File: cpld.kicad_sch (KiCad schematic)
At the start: 30 parts, among them IC1 MCP1726-3302E_SN, IC2 EPM3064ATC44-7N, J1 USB_OTG, J2 INPUTS, J3 OUTPUTS, J4 Conn_ARM_JTAG_SWD_10, SW1 POWER_SW, SW2 SW_DIP_x01, SW3 SW_DIP_x01, SW4 SW_DIP_x01, SW5 SW_DIP_x01, Y1 ECS-2033-500-BN-TR3

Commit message: Added revision and title
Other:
- company: (none) -> AGH UST
- title: (none) -> ATPG with CPLD circuit
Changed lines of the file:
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@@
 (kicad_sch (version 20211123) (generator eeschema)
   (paper "A4")
+  (title_block
+    (title "ATPG with CPLD circuit")
+    (date "2022-08-07")
+    (rev "0.0.1")
+    (company "AGH UST")
+    (comment 1 "Author: Radosław Sajdak")
+  )
   (junction (at 104.14 177.8) (diameter 0) (color 0 0 0 0)
   )

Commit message: Final PCB
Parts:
- removed J2: INPUTS, Connector_PinSocket_2.54mm:PinSocket_2x16_P2.54mm_Vertical, symbol Connector_Generic:Conn_02x16_Top_Bottom
- removed J3: OUTPUTS, Connector_PinSocket_2.54mm:PinSocket_2x16_P2.54mm_Vertical, symbol Connector_Generic:Conn_02x16_Top_Bottom
- removed Y1: ECS-2033-500-BN-TR3, ECS2033:ECS2033500BNTR3, symbol ECS-2033-500-BN-TR3:ECS-2033-500-BN-TR3
- added C9: 0.1u, Capacitor_SMD:C_0603_1608Metric, symbol Device:C
- added J2: INPUTS, Connector_PinSocket_2.54mm:PinSocket_2x16_P2.54mm_Vertical_SMD, symbol Connector_Generic:Conn_02x16_Odd_Even
- added J3: OUTPUTS, Connector_PinSocket_2.54mm:PinSocket_2x16_P2.54mm_Vertical_SMD, symbol Connector_Generic:Conn_02x16_Odd_Even
- added Y1: ECS-TXO-3225-250-TR, ECS_3225:OSC_ECS-TXO-3225-250-TR, symbol ECS-TXO-3225-250-TR:ECS-TXO-3225-250-TR
- C2: value 1000p -> 1u
- renumbered SW2 to SW0, SW3 to SW1, SW4 to SW2, SW5 to SW3, SW1 to SW_POW1
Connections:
- net DI0 is gone; now on net DI1: IC2.2 (I/O_1)
- net DI5 is gone; now on net DI7: IC2.10 (I/O_6)
- net DO6 is gone; now on net DO5: IC2.25 (I/O_17)
- net +3.3V: now also C9.2, Y1.4 (VDD)
- net DI1: now also J2.3 (Pin_3); no longer IC2.3 (I/O_2)
- net DI2: now also IC2.3 (I/O_2), J2.5 (Pin_5); no longer IC2.5 (I/O_3)
- net DI3: now also IC2.5 (I/O_3), J2.7 (Pin_7); no longer IC2.6 (I/O_4)
- net DI4: now also IC2.6 (I/O_4), J2.9 (Pin_9); no longer IC2.8 (I/O_5)
- net DI6: now also IC2.8 (I/O_5), J2.13 (Pin_13); no longer IC2.12 (I/O_7)
- net DI7: now also J2.15 (Pin_15); no longer IC2.13 (I/O_8)
- net DI8: now also IC2.12 (I/O_7), J2.17 (Pin_17); no longer IC2.14 (I/O_9)
- net DI9: now also IC2.13 (I/O_8), J2.19 (Pin_19); no longer IC2.15 (I/O_10)
- net DO0: now also IC2.19 (I/O_12), J3.1 (Pin_1); no longer IC2.18 (I/O_11)
- net DO1: now also IC2.20 (I/O_13), J3.3 (Pin_3); no longer IC2.19 (I/O_12)
- net DO2: now also IC2.21 (I/O_14), J3.5 (Pin_5); no longer IC2.20 (I/O_13)
- net DO3: now also IC2.22 (I/O_15), J3.7 (Pin_7); no longer IC2.21 (I/O_14)
- net DO4: now also IC2.23 (I/O_16), J3.9 (Pin_9); no longer IC2.22 (I/O_15)
- net DO5: now also J3.11 (Pin_11); no longer IC2.23 (I/O_16)
- net DO7: now also J3.15 (Pin_15)
- net DO8: now also J3.17 (Pin_17); no longer IC2.28 (I/O_19)
- net DO9: now also IC2.28 (I/O_19), J3.19 (Pin_19); no longer IC2.31 (I/O_20)
- net GND: now also R6.2, R7.2, C9.1, J2.10 (Pin_10), J2.12 (Pin_12), J2.14 (Pin_14), J2.16 (Pin_16), J2.18 (Pin_18), J2.2 (Pin_2), J2.20 (Pin_20), J2.22 (Pin_22), J2.24 (Pin_24), J2.26 (Pin_26), J2.28 (Pin_28), J2.30 (Pin_30), J2.32 (Pin_32), J2.4 (Pin_4), J2.6 (Pin_6), J2.8 (Pin_8), J3.10 (Pin_10), J3.12 (Pin_12), J3.14 (Pin_14), J3.16 (Pin_16), J3.18 (Pin_18), J3.2 (Pin_2), J3.20 (Pin_20), J3.22 (Pin_22), J3.24 (Pin_24), J3.26 (Pin_26), J3.28 (Pin_28), J3.30 (Pin_30), J3.32 (Pin_32), J3.4 (Pin_4), J3.6 (Pin_6), J3.8 (Pin_8), Y1.2 (GND); no longer D1.1 (K), D2.1 (K)
- net POWER_LED: now also D1.2 (A); no longer R6.1
- net STATUS_LED: now also D2.2 (A), IC2.34 (I/O_22); no longer R7.1
- net SW_B0: now also IC2.35 (I/O_23); no longer IC2.34 (I/O_22)
- net SW_B1: now also IC2.42 (I/O_24); no longer IC2.35 (I/O_23)
- net SW_B2: now also IC2.43 (I/O_25); no longer IC2.42 (I/O_24)
- net SW_B3: now also IC2.44 (I/O_26); no longer IC2.43 (I/O_25)
- net DO12: now reaches IC2.33 (I/O_21)
- net DO12: now also J3.25 (Pin_25)
- net at IC2.37 (INPUT/GCLK1): now also Y1.3 (OUTPUT)
- net TCK renamed DO6/TCK
- net DO6/TCK: now also J3.13 (Pin_13)
- net TDI renamed DI0/TDI
- net DI0/TDI: now also J2.1 (Pin_1)
- net TDO renamed DO11/TDO
- net DO11/TDO: now also J3.23 (Pin_23)
- net TMS renamed DI5/TMS
- net DI5/TMS: now also J2.11 (Pin_11)
- new net: D2.1 (K), R7.1
- new net: D1.1 (K), R6.1
- new net DI10: IC2.14 (I/O_9), J2.21 (Pin_21)
- new net DI11: IC2.15 (I/O_10), J2.23 (Pin_23)
- new net DI12: IC2.18 (I/O_11), J2.25 (Pin_25)
- new net DO10: IC2.31 (I/O_20), J3.21 (Pin_21)
- no-connect marks 23 -> 14
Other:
- moved on the sheet: D1, D2, R6, R7

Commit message: Improved PCB layout
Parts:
- J4: footprint Connector_PinSocket_2.54mm:PinSocket_2x05_P2.54mm_Vertical -> Connector_PinSocket_2.54mm:PinSocket_2x05_P2.54mm_Vertical_SMD
- renumbered SW3 to SW0, SW2 to SW1, SW1 to SW2, SW0 to SW3
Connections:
- net +5V: now also D1.2 (A)
- net DO12: now also IC2.34 (I/O_22); no longer IC2.33 (I/O_21)
- net DO8: now also IC2.28 (I/O_19)
- net DO9: now also IC2.31 (I/O_20); no longer IC2.28 (I/O_19)
- net STATUS_LED: now also IC1.5 (PWRGD); no longer IC2.34 (I/O_22)
- net SW_B0: now also IC2.44 (I/O_26), SW0.2; no longer IC2.35 (I/O_23), SW3.2
- net SW_B1: now also IC2.43 (I/O_25), SW1.2; no longer IC2.42 (I/O_24), SW2.2
- net SW_B2: now also IC2.42 (I/O_24), SW2.2; no longer IC2.43 (I/O_25), SW1.2
- net SW_B3: now also IC2.35 (I/O_23), SW3.2; no longer IC2.44 (I/O_26), SW0.2
- net DO10 renamed DO10/TDO
- net DO10/TDO: now also IC2.32 (I/O/TDO), R2.2, R4.2; no longer IC2.31 (I/O_20)
- removed net DO11/TDO: IC2.32 (I/O/TDO), J3.23 (Pin_23), R2.2, R4.2
- removed net POWER_LED: D1.2 (A), IC1.5 (PWRGD)
- new net DO11: IC2.33 (I/O_21), J3.23 (Pin_23)
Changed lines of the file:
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@@
-    (stroke (width 0) (type default) (color 0 0 0 0))
-  )
-  (wire (pts (xy 85.09 38.1) (xy 87.63 38.1))
     (stroke (width 0) (type default) (color 0 0 0 0))
   )
@@
     (effects (font (size 1.27 1.27)) (justify left bottom))
   )
-  (label "DO9" (at 210.82 116.84 0)
+  (label "DO8" (at 210.82 116.84 0)
     (effects (font (size 1.27 1.27)) (justify left bottom))
   )
@@
     (effects (font (size 1.27 1.27)) (justify right bottom))
   )
-  (label "SW_B0" (at 200.66 73.66 90)
+  (label "SW_B3" (at 200.66 73.66 90)
     (effects (font (size 1.27 1.27)) (justify left bottom))
   )
@@
     (effects (font (size 1.27 1.27)) (justify right bottom))
   )
-  (label "DO10" (at 210.82 109.22 0)
+  (label "DO10{slash}TDO" (at 210.82 106.68 0)
     (effects (font (size 1.27 1.27)) (justify left bottom))
   )
   (label "DO6{slash}TCK" (at 135.89 104.14 0)
+    (effects (font (size 1.27 1.27)) (justify left bottom))
+  )
+  (label "STATUS_LED" (at 85.09 38.1 0)
     (effects (font (size 1.27 1.27)) (justify left bottom))
   )
@@
     (effects (font (size 1.27 1.27)) (justify left bottom))
   )
-  (label "SW_B1" (at 182.88 73.66 90)
+  (label "SW_B2" (at 182.88 73.66 90)
     (effects (font (size 1.27 1.27)) (justify left bottom))
   )
@@
     (effects (font (size 1.27 1.27)) (justify left bottom))
   )
-  (label "POWER_LED" (at 87.63 38.1 0)
+  (label "POWER_LED" (at 35.56 27.94 0)
     (effects (font (size 1.27 1.27)) (justify left bottom))
   )
@@
     (effects (font (size 1.27 1.27)) (justify right bottom))
   )
-  (label "SW_B3" (at 177.8 73.66 90)
+  (label "SW_B0" (at 177.8 73.66 90)
     (effects (font (size 1.27 1.27)) (justify left bottom))
   )
@@
     (effects (font (size 1.27 1.27)) (justify right bottom))
   )
-  (label "DO11{slash}TDO" (at 210.82 106.68 0)
+  (label "DO11" (at 210.82 104.14 0)
     (effects (font (size 1.27 1.27)) (justify left bottom))
   )
@@
     (effects (font (size 1.27 1.27)) (justify right bottom))
   )
-  (label "STATUS_LED" (at 203.2 73.66 90)
-    (effects (font (size 1.27 1.27)) (justify left bottom))
-  )
   (label "DO3" (at 203.2 147.32 270)
     (effects (font (size 1.27 1.27)) (justify right bottom))
@@
     (effects (font (size 1.27 1.27)) (justify right bottom))
   )
-  (label "SW_B2" (at 180.34 73.66 90)
-    (effects (font (size 1.27 1.27)) (justify left bottom))
-  )
-  (label "DO11{slash}TDO" (at 135.89 109.22 0)
-    (effects (font (size 1.27 1.27)) (justify left bottom))
-  )
-  (label "DO12" (at 210.82 104.14 0)
-    (effects (font (size 1.27 1.27)) (justify left bottom))
-  )
-  (hierarchical_label "DO11{slash}TDO" (shape output) (at 27.94 167.64 180)
+  (label "SW_B1" (at 180.34 73.66 90)
+    (effects (font (size 1.27 1.27)) (justify left bottom))
+  )
+  (label "DO10{slash}TDO" (at 135.89 109.22 0)
+    (effects (font (size 1.27 1.27)) (justify left bottom))
+  )
+  (label "DO12" (at 203.2 73.66 90)
+    (effects (font (size 1.27 1.27)) (justify left bottom))
+  )
+  (label "DO9" (at 210.82 109.22 0)
+    (effects (font (size 1.27 1.27)) (justify left bottom))
+  )
+  (hierarchical_label "DO11" (shape output) (at 27.94 167.64 180)
     (effects (font (size 1.27 1.27)) (justify right))
   )
@@
     (effects (font (size 1.27 1.27)) (justify right))
   )
-  (hierarchical_label "SW_B1" (shape input) (at 119.38 161.29 0)
+  (hierarchical_label "SW_B2" (shape input) (at 119.38 161.29 0)
     (effects (font (size 1.27 1.27)) (justify left))
   )
-  (hierarchical_label "SW_B2" (shape input) (at 119.38 170.18 0)
+  (hierarchical_label "SW_B1" (shape input) (at 119.38 170.18 0)
     (effects (font (size 1.27 1.27)) (justify left))
   )
@@
     (effects (font (size 1.27 1.27)) (justify right))
   )
-  (hierarchical_label "DO10" (shape output) (at 27.94 165.1 180)
+  (hierarchical_label "DO10{slash}TDO" (shape output) (at 27.94 165.1 180)
     (effects (font (size 1.27 1.27)) (justify right))
   )
@@
     (effects (font (size 1.27 1.27)) (justify right))
   )
-  (hierarchical_label "SW_B3" (shape input) (at 119.38 177.8 0)
+  (hierarchical_label "SW_B0" (shape input) (at 119.38 177.8 0)
     (effects (font (size 1.27 1.27)) (justify left))
   )
@@
     (effects (font (size 1.27 1.27)) (justify right))
   )
-  (hierarchical_label "SW_B0" (shape input) (at 119.38 152.4 0)
+  (hierarchical_label "SW_B3" (shape input) (at 119.38 152.4 0)
     (effects (font (size 1.27 1.27)) (justify left))
   )
@@
   (symbol (lib_id "Switch:SW_DIP_x01") (at 111.76 152.4 0) (unit 1)
     (in_bom yes) (on_board yes) (fields_autoplaced)
-    (property "Reference" "SW0" (id 0) (at 111.76 144.78 0))
+    (property "Reference" "SW3" (id 0) (at 111.76 144.78 0))
     (property "Value" "SW_DIP_x01" (id 1) (at 111.76 147.32 0))
     (property "Footprint" "Button_Switch_THT:SW_DIP_SPSTx01_Slide_9.78x4.72mm_W7.62mm_P2.54mm" (id 2) (at 111.76 152.4 0)
@@
   (symbol (lib_id "Switch:SW_DIP_x01") (at 111.76 177.8 0) (unit 1)
     (in_bom yes) (on_board yes) (fields_autoplaced)
-    (property "Reference" "SW3" (id 0) (at 111.76 170.18 0))
+    (property "Reference" "SW0" (id 0) (at 111.76 170.18 0))
     (property "Value" "SW_DIP_x01" (id 1) (at 111.76 172.72 0))
     (property "Footprint" "Button_Switch_THT:SW_DIP_SPSTx01_Slide_9.78x4.72mm_W7.62mm_P2.54mm" (id 2) (at 111.76 177.8 0)
@@
       (effects (font (size 1.27 1.27)) (justify right))
     )
-    (property "Footprint" "Connector_PinSocket_2.54mm:PinSocket_2x05_P2.54mm_Vertical" (id 2) (at 100.33 106.68 0)
+    (property "Footprint" "Connector_PinSocket_2.54mm:PinSocket_2x05_P2.54mm_Vertical_SMD" (id 2) (at 100.33 106.68 0)
       (effects (font (size 1.27 1.27)) hide)
     )
@@
   (symbol (lib_id "Switch:SW_DIP_x01") (at 111.76 161.29 0) (unit 1)
     (in_bom yes) (on_board yes) (fields_autoplaced)
-    (property "Reference" "SW1" (id 0) (at 111.76 153.67 0))
+    (property "Reference" "SW2" (id 0) (at 111.76 153.67 0))
     (property "Value" "SW_DIP_x01" (id 1) (at 111.76 156.21 0))
     (property "Footprint" "Button_Switch_THT:SW_DIP_SPSTx01_Slide_9.78x4.72mm_W7.62mm_P2.54mm" (id 2) (at 111.76 161.29 0)
@@
   (symbol (lib_id "Switch:SW_DIP_x01") (at 111.76 170.18 0) (unit 1)
     (in_bom yes) (on_board yes) (fields_autoplaced)
-    (property "Reference" "SW2" (id 0) (at 111.76 162.56 0))
+    (property "Reference" "SW1" (id 0) (at 111.76 162.56 0))
     (property "Value" "SW_DIP_x01" (id 1) (at 111.76 165.1 0))
     (property "Footprint" "Button_Switch_THT:SW_DIP_SPSTx01_Slide_9.78x4.72mm_W7.62mm_P2.54mm" (id 2) (at 111.76 170.18 0)
@@
     )
     (path "/5972ed6a-d198-4093-859d-ce06eea4ab68"
-      (reference "J4") (unit 1) (value "Conn_ARM_JTAG_SWD_10") (footprint "Connector_PinSocket_2.54mm:PinSocket_2x05_P2.54mm_Vertical")
+      (reference "J4") (unit 1) (value "Conn_ARM_JTAG_SWD_10") (footprint "Connector_PinSocket_2.54mm:PinSocket_2x05_P2.54mm_Vertical_SMD")
     )
     (path "/cbeb8967-359e-4c45-b3f9-fe5a1c99a245"
@@
       (reference "R8") (unit 1) (value "68") (footprint "Resistor_SMD:R_0603_1608Metric")
     )
+    (path "/276a6b66-0589-4239-a482-0d9cf1aa6608"
+      (reference "SW0") (unit 1) (value "SW_DIP_x01") (footprint "Button_Switch_THT:SW_DIP_SPSTx01_Slide_9.78x4.72mm_W7.62mm_P2.54mm")
+    )
+    (path "/bad29623-ecf2-4987-8d17-41e74aba39de"
+      (reference "SW1") (unit 1) (value "SW_DIP_x01") (footprint "Button_Switch_THT:SW_DIP_SPSTx01_Slide_9.78x4.72mm_W7.62mm_P2.54mm")
+    )
+    (path "/a2d6326b-416c-423f-8398-5ee639c925a8"
+      (reference "SW2") (unit 1) (value "SW_DIP_x01") (footprint "Button_Switch_THT:SW_DIP_SPSTx01_Slide_9.78x4.72mm_W7.62mm_P2.54mm")
+    )
     (path "/094f38df-83ad-4d33-9082-551f27f4b9ab"
-      (reference "SW0") (unit 1) (value "SW_DIP_x01") (footprint "Button_Switch_THT:SW_DIP_SPSTx01_Slide_9.78x4.72mm_W7.62mm_P2.54mm")
-    )
-    (path "/a2d6326b-416c-423f-8398-5ee639c925a8"
-      (reference "SW1") (unit 1) (value "SW_DIP_x01") (footprint "Button_Switch_THT:SW_DIP_SPSTx01_Slide_9.78x4.72mm_W7.62mm_P2.54mm")
-    )
-    (path "/bad29623-ecf2-4987-8d17-41e74aba39de"
-      (reference "SW2") (unit 1) (value "SW_DIP_x01") (footprint "Button_Switch_THT:SW_DIP_SPSTx01_Slide_9.78x4.72mm_W7.62mm_P2.54mm")
-    )
-    (path "/276a6b66-0589-4239-a482-0d9cf1aa6608"
       (reference "SW3") (unit 1) (value "SW_DIP_x01") (footprint "Button_Switch_THT:SW_DIP_SPSTx01_Slide_9.78x4.72mm_W7.62mm_P2.54mm")
     )

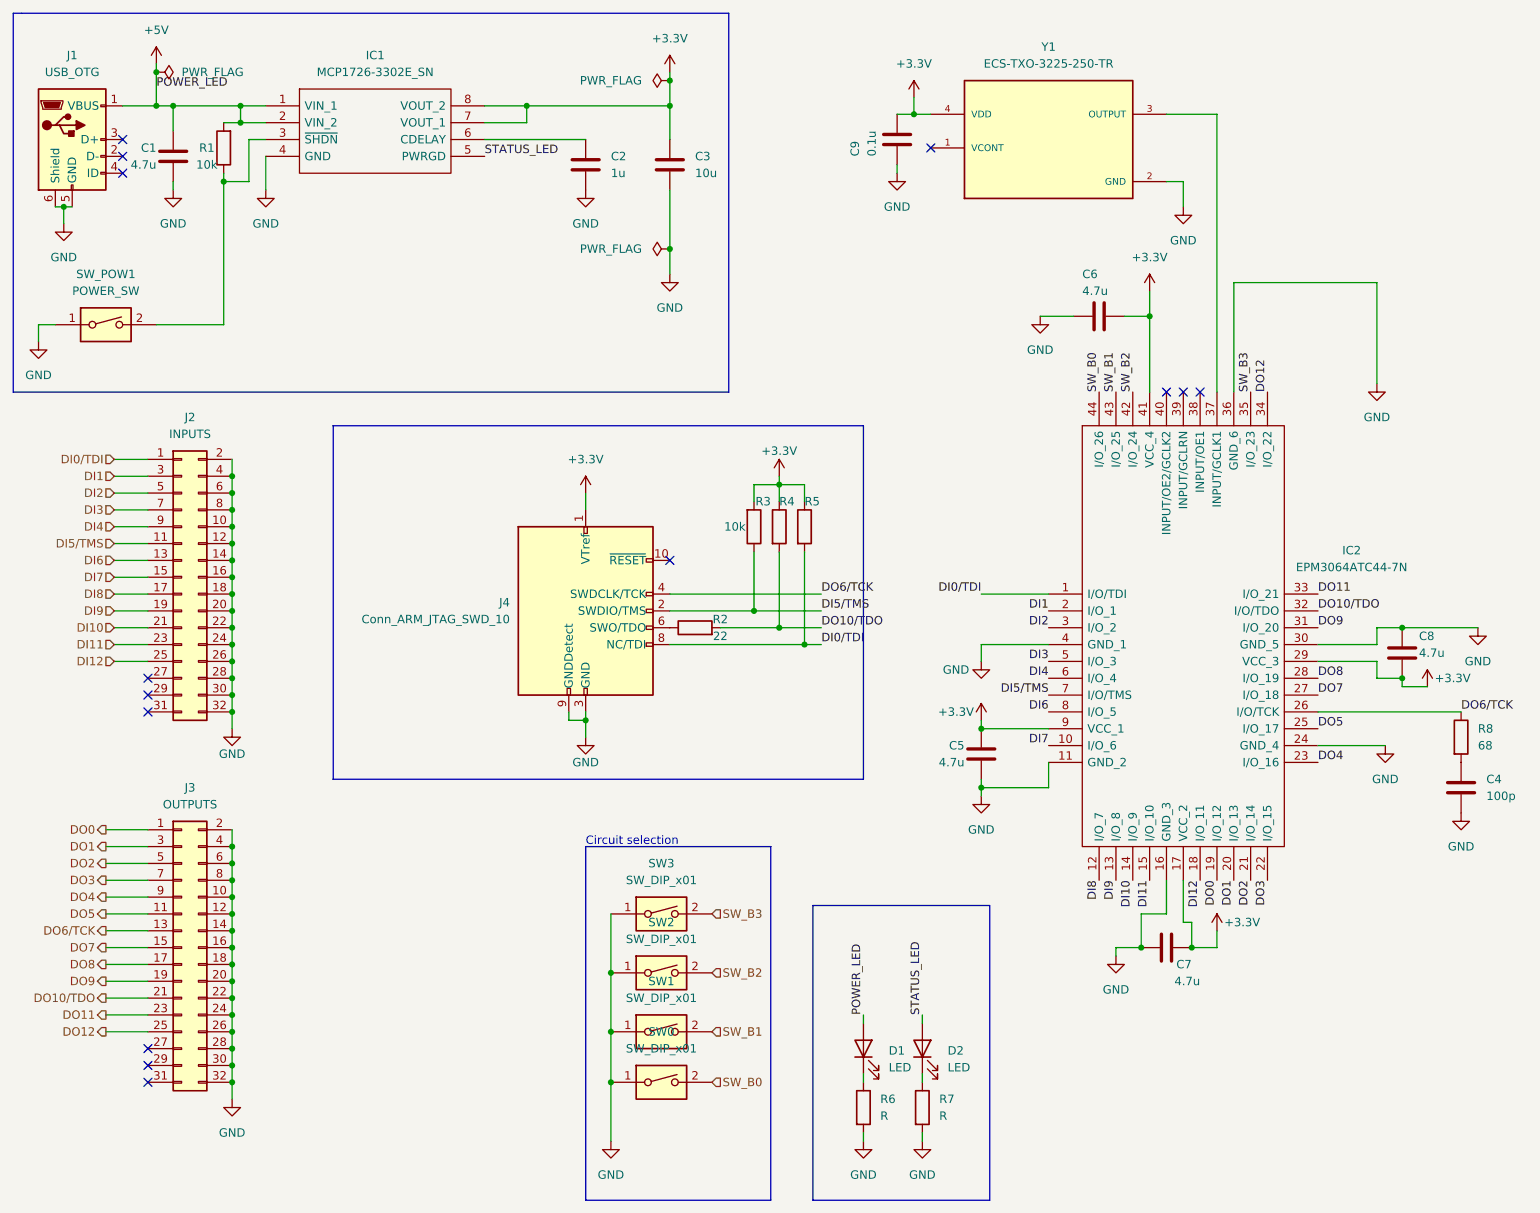
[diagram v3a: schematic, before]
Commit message: Changed connectors and LDO
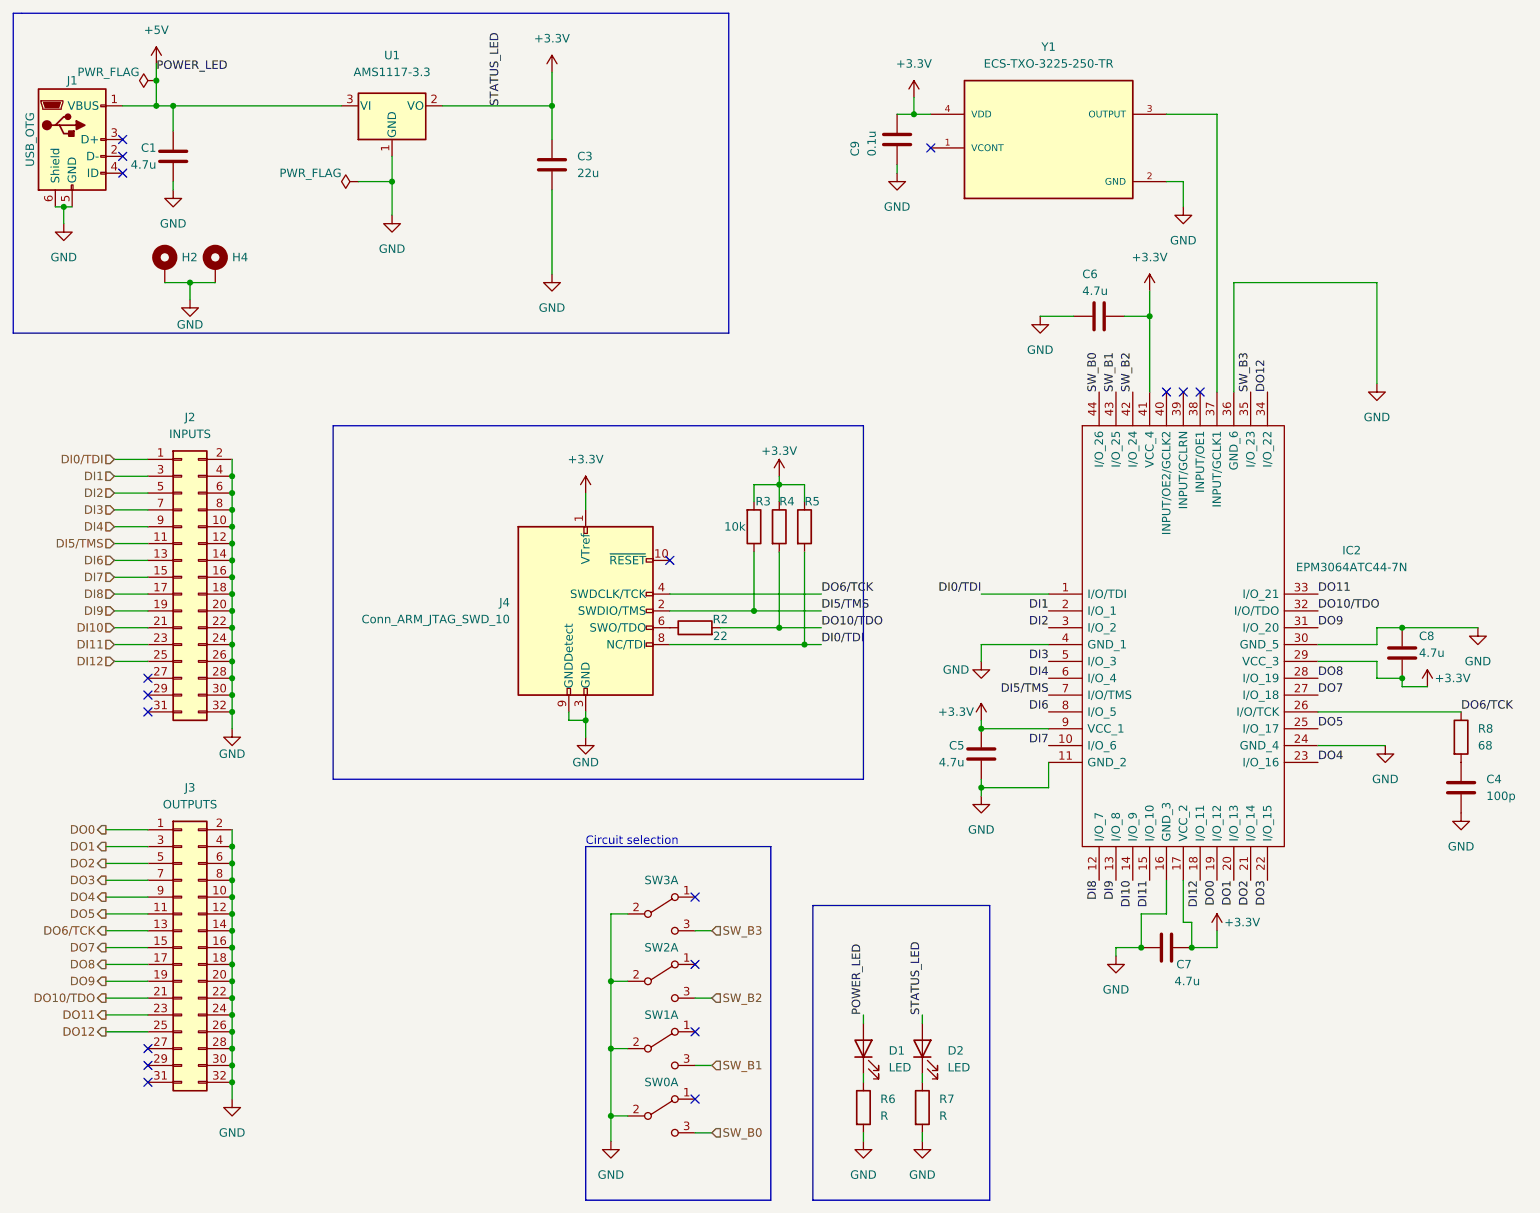
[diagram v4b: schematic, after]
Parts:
- removed C2: 1u, Capacitor_SMD:C_0603_1608Metric, symbol Device:C
- removed IC1: MCP1726-3302E_SN, MCP1726:SOIC127P600X175-8N, symbol MCP1726-3302E_SN:MCP1726-3302E_SN
- removed R1: 10k, Resistor_SMD:R_0603_1608Metric, symbol Device:R
- removed SW0, SW1, SW2, SW3: SW_DIP_x01, Button_Switch_THT:SW_DIP_SPSTx01_Slide_9.78x4.72mm_W7.62mm_P2.54mm, symbol Switch:SW_DIP_x01
- removed SW_POW1: POWER_SW, Button_Switch_THT:SW_DIP_SPSTx01_Slide_9.78x4.72mm_W7.62mm_P2.54mm, symbol Switch:SW_DIP_x01
- added H2, H4: MountingHole_Pad, MountingHole:MountingHole_3.2mm_M3_DIN965_Pad_TopBottom, symbol Mechanical:MountingHole_Pad
- added SW0, SW1, SW2, SW3: SW_DPDT_x2, Button_Switch_THT:SW_E-Switch_EG1271_DPDT, symbol Switch:SW_DPDT_x2
- added U1: AMS1117-3.3, Package_TO_SOT_SMD:SOT-223-3_TabPin2, symbol Regulator_Linear:AMS1117-3.3
- C3: value 10u -> 22u
- J2, J3: footprint Connector_PinSocket_2.54mm:PinSocket_2x16_P2.54mm_Vertical_SMD -> Connector_PinSocket_2.54mm:PinSocket_2x16_P2.54mm_Vertical
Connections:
- net STATUS_LED is gone; now on net +3.3V: D2.2 (A)
- net +3.3V: now also U1.2 (VO)
- net +5V: now also U1.3 (VI)
- net GND: now also H2.1, H4.1, SW0.2 (B), SW1.2 (B), SW2.2 (B), SW3.2 (B), U1.1 (GND)
- net SW_B0: now also SW0.3 (C)
- net SW_B1: now also SW1.3 (C)
- net SW_B2: now also SW2.3 (C)
- net SW_B3: now also SW3.3 (C)
- no-connect marks 14 -> 18
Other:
- moved on the sheet: C3
